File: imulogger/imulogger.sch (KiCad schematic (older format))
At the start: 28 parts, among them J1 DEBUG, J2 BATCONN, J3 CHGCONN, J4 Micro_SD_Card, SW1 SW_SPDT, U1 ESP32-WROOM-32, U2 USFS, U3 MCP1826S, U5 dw01, U6 FS8205A

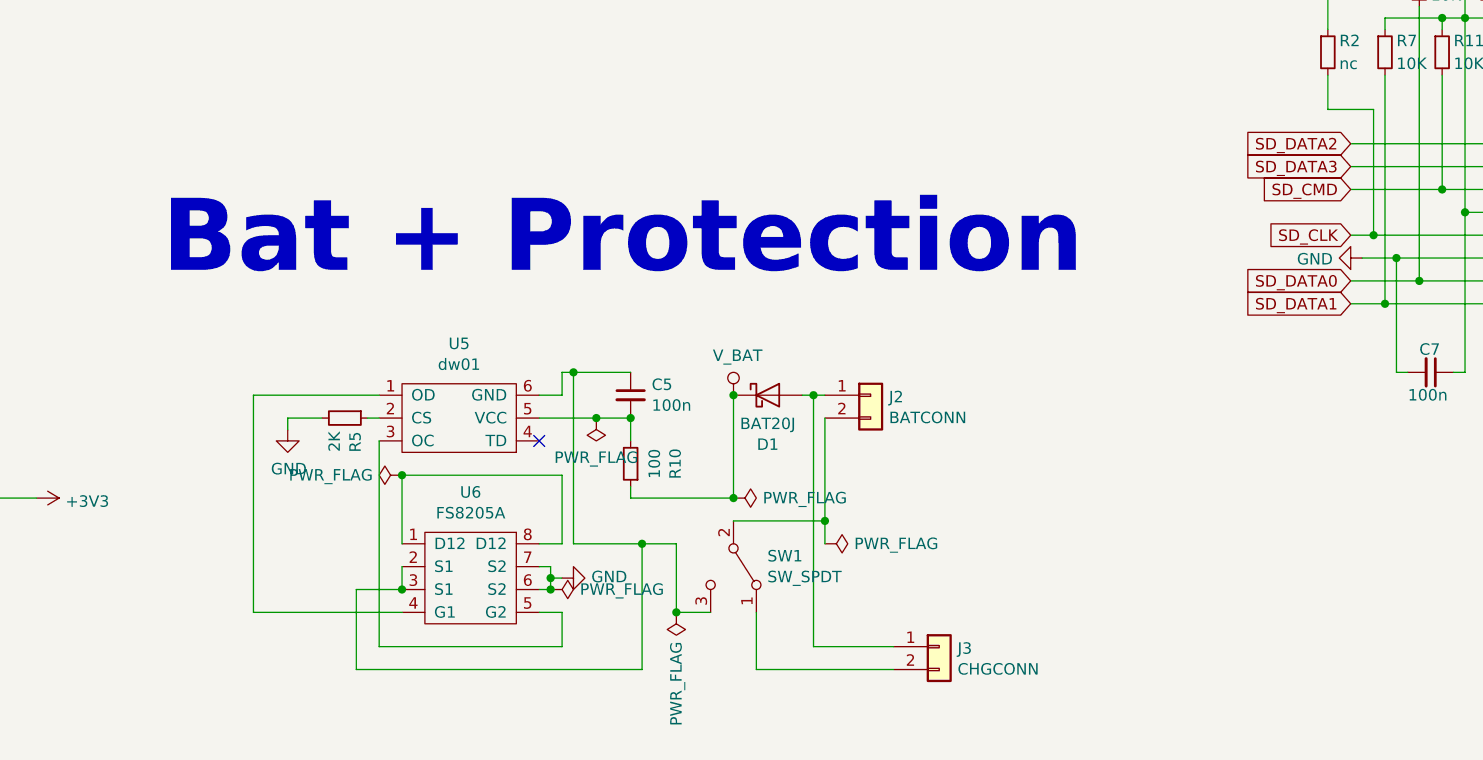
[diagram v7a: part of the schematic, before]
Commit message: remove battery protection circuit
my battery has that already and even if I had one without one
it'd be easier to buy one and glue it to the battery than soldering
these small ICs.
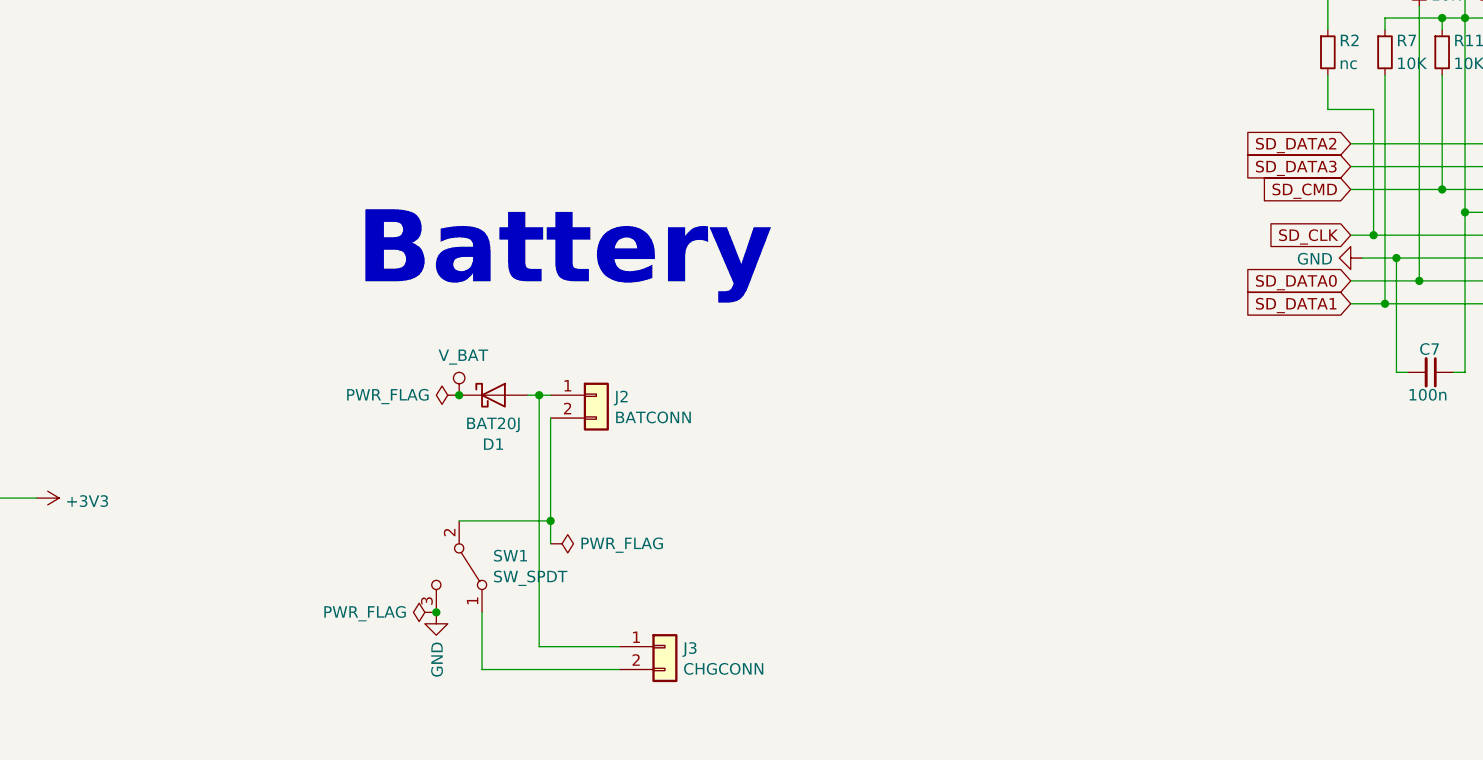
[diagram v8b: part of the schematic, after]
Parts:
- removed C5: 100n, Capacitor_SMD:C_0805_2012Metric_Pad1.15x1.40mm_HandSolder, symbol Device:C_Small
- removed R10: 100, Resistor_SMD:R_0805_2012Metric_Pad1.15x1.40mm_HandSolder, symbol Device:R_Small
- removed R5: 2K, Resistor_SMD:R_0805_2012Metric_Pad1.15x1.40mm_HandSolder, symbol Device:R_Small
- removed U5: dw01, Package_TO_SOT_SMD:SOT-23-6_Handsoldering, symbol imulogger-symbols:dw01
- removed U6: FS8205A, Package_SO:TSSOP-8_4.4x3mm_P0.65mm, symbol imulogger-symbols:FS8205A
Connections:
- net GND: now also SW1.3 (C)
- no-connect marks 31 -> 30
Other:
- note added: "Battery"
- note removed: "Bat + Protection"
- moved on the sheet: D1, J2, J3, SW1
